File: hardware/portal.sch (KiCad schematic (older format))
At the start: 19 parts, among them J1 Screw_Terminal_1x02, J10 Screw_Terminal_1x02, J11 Screw_Terminal_1x02, J2 Screw_Terminal_1x02, J3 Raspberry_Pi_2_3, J4 CONN_01X01, J5 CONN_01X01, J6 CONN_01X01, J7 CONN_01X01, J8 Screw_Terminal_1x02, U1 PC817, U2 PC817

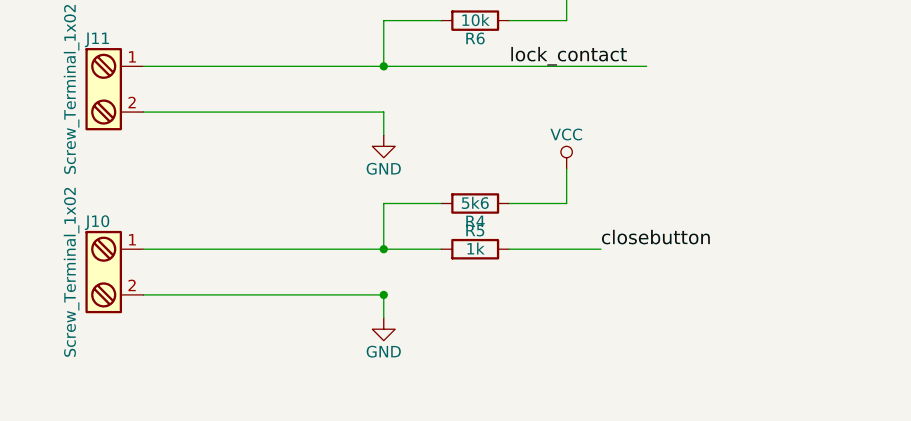
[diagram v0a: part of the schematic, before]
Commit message: Added debouncing to the PCB and widened the traces
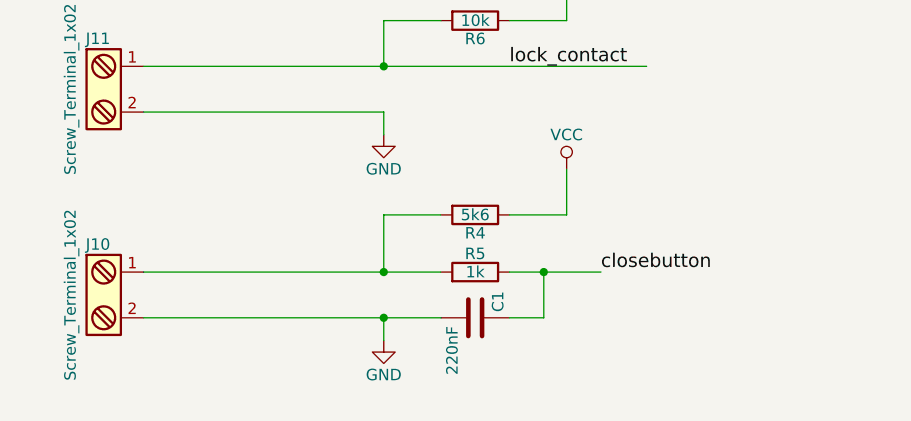
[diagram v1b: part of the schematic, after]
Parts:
- added C1: 220nF, Capacitors_SMD:C_0805_HandSoldering, symbol C
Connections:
- wire segments 46 -> 48
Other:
- moved on the sheet: J10, R4, R5
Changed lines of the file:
@@
 	2250 4900 3300 4900
 Wire Wire Line
-	2250 6450 3550 6450
+	2250 6550 3550 6550
 Text Label 3850 4050 0    60   ~ 0
 reed_contact
@@
 Text Label 2450 4900 0    60   ~ 0
 beeper
-Text Label 4250 6450 0    60   ~ 0
+Text Label 4250 6550 0    60   ~ 0
 closebutton
 $Comp
@@
 L Screw_Terminal_1x02 J10
 U 1 1 59AC1DB0
-P 2050 6550
-F 0 "J10" H 2050 6800 50  0000 C TNN
-F 1 "Screw_Terminal_1x02" V 1900 6550 50  0000 C TNN
-F 2 "SparkFun-Connectors:SCREWTERMINAL-5MM-2" H 2050 6325 50  0001 C CNN
-F 3 "" H 2025 6550 50  0001 C CNN
-	1    2050 6550
+P 2050 6650
+F 0 "J10" H 2050 6900 50  0000 C TNN
+F 1 "Screw_Terminal_1x02" V 1900 6650 50  0000 C TNN
+F 2 "SparkFun-Connectors:SCREWTERMINAL-5MM-2" H 2050 6425 50  0001 C CNN
+F 3 "" H 2025 6650 50  0001 C CNN
+	1    2050 6650
 	1    0    0    -1
 $EndComp
@@
 	3300 5850 3300 5950
 Wire Wire Line
-	3300 6650 3300 6750
+	3300 6750 3300 6850
 $Comp
 L GND #PWR03
@@
 L GND #PWR06
 U 1 1 59AC2065
-P 3300 6750
-F 0 "#PWR06" H 3300 6500 50  0001 C CNN
-F 1 "GND" H 3300 6600 50  0000 C CNN
-F 2 "" H 3300 6750 50  0001 C CNN
-F 3 "" H 3300 6750 50  0001 C CNN
-	1    3300 6750
+P 3300 6850
+F 0 "#PWR06" H 3300 6600 50  0001 C CNN
+F 1 "GND" H 3300 6700 50  0000 C CNN
+F 2 "" H 3300 6850 50  0001 C CNN
+F 3 "" H 3300 6850 50  0001 C CNN
+	1    3300 6850
 	1    0    0    -1
 $EndComp
@@
 	1    0    0    -1
 $EndComp
-Wire Wire Line
-	4100 6100 4100 6250
-Wire Wire Line
-	3300 6450 3300 6250
 $Comp
 L R R4
 U 1 1 59AC4311
-P 3700 6250
-F 0 "R4" V 3780 6250 50  0000 C CNN
-F 1 "5k6" V 3700 6250 50  0000 C CNN
-F 2 "Resistors_SMD:R_0805_HandSoldering" V 3630 6250 50  0001 C CNN
-F 3 "" H 3700 6250 50  0001 C CNN
-	1    3700 6250
-	0    1    1    0
-$EndComp
-Wire Wire Line
-	4100 6250 3850 6250
-Wire Wire Line
-	3300 6250 3550 6250
-Connection ~ 3300 6450
+P 3700 6300
+F 0 "R4" V 3780 6300 50  0000 C CNN
+F 1 "5k6" V 3700 6300 50  0000 C CNN
+F 2 "Resistors_SMD:R_0805_HandSoldering" V 3630 6300 50  0001 C CNN
+F 3 "" H 3700 6300 50  0001 C CNN
+	1    3700 6300
+	0    1    1    0
+$EndComp
+Wire Wire Line
+	4100 6300 3850 6300
+Wire Wire Line
+	3300 6300 3550 6300
+Connection ~ 3300 6550
 $Comp
 L R R5
 U 1 1 59AC45E1
-P 3700 6450
-F 0 "R5" V 3780 6450 50  0000 C CNN
-F 1 "1k" V 3700 6450 50  0000 C CNN
-F 2 "Resistors_SMD:R_0805_HandSoldering" V 3630 6450 50  0001 C CNN
-F 3 "" H 3700 6450 50  0001 C CNN
-	1    3700 6450
+P 3700 6550
+F 0 "R5" V 3780 6550 50  0000 C CNN
+F 1 "1k" V 3700 6550 50  0000 C CNN
+F 2 "Resistors_SMD:R_0805_HandSoldering" V 3630 6550 50  0001 C CNN
+F 3 "" H 3700 6550 50  0001 C CNN
+	1    3700 6550
 	0    1    -1   0
 $EndComp
@@
 	-1   0    0    1
 $EndComp
-Connection ~ 3300 6650
-Wire Wire Line
-	4250 6450 3850 6450
-Wire Wire Line
-	2250 6650 3300 6650
+Connection ~ 3300 6750
+Wire Wire Line
+	4250 6550 3850 6550
+Wire Wire Line
+	2250 6750 3550 6750
+Wire Wire Line
+	4100 6100 4100 6300
+Wire Wire Line
+	3300 6300 3300 6550
+$Comp
+L C C1
+U 1 1 5AEF1FF5
+P 3700 6750
+F 0 "C1" H 3725 6850 50  0000 L CNN
+F 1 "220nF" H 3450 6650 50  0000 L CNN
+F 2 "Capacitors_SMD:C_0805_HandSoldering" H 3738 6600 50  0001 C CNN
+F 3 "" H 3700 6750 50  0001 C CNN
+	1    3700 6750
+	0    1    -1   0
+$EndComp
+Wire Wire Line
+	3850 6750 4000 6750
+Wire Wire Line
+	4000 6750 4000 6550
+Connection ~ 4000 6550
 $EndSCHEMATC
